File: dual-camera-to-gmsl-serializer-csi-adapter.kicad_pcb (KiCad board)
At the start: 4 copper layers, 101.2 x 43 mm, 85 parts, among them J1 Conn_FFC_WE_68715014022, J2 Conn_FFC_WE_68715014022, J3 Conn_FFC_WE_68715014022, U1 TPS2117DRLR, U2 TPS2117DRLR, U3 AP62301_TSOT

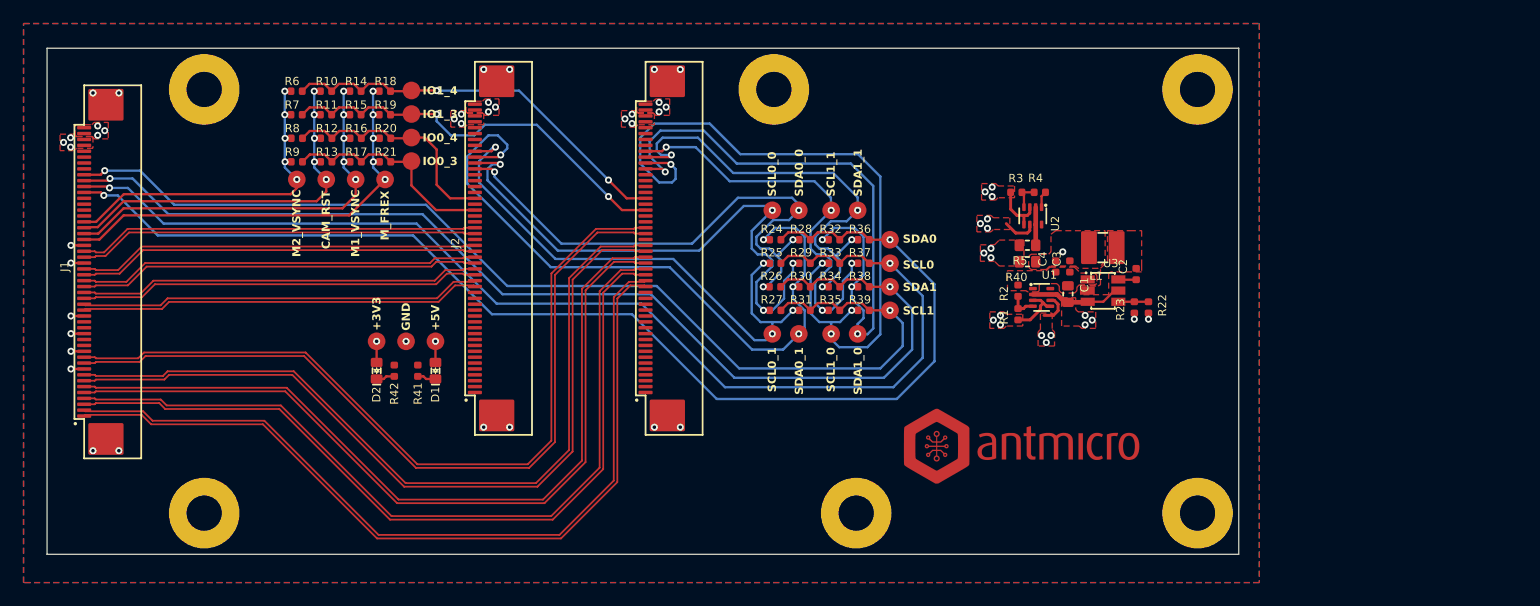
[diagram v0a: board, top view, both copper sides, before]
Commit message: [#69172] Rotate FFC connectors
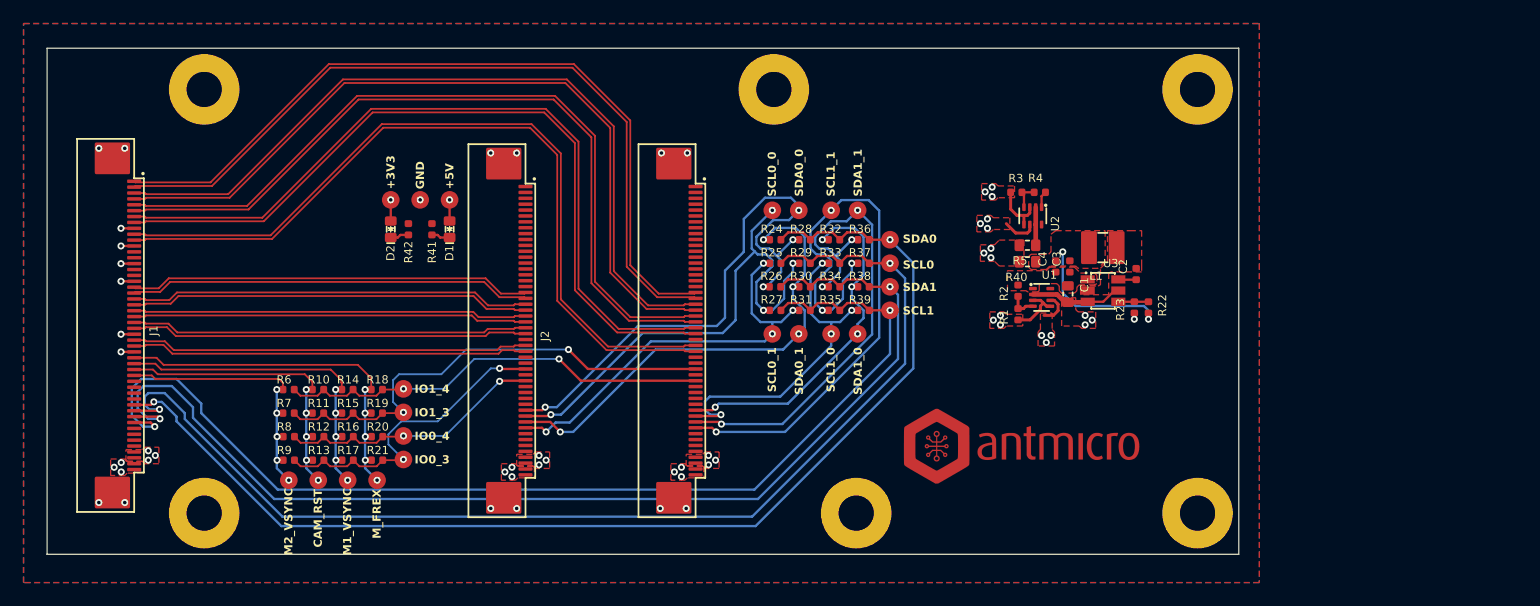
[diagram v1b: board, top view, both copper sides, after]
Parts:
- moved TP1 25.6 mm to (120.0, 116.3)
- moved TP2 25.6 mm to (122.5, 116.3)
- moved TP3 25.6 mm to (125.0, 116.3)
- moved TP4 25.6 mm to (127.5, 116.3)
- moved TP5 25.4 mm to (129.8, 108.5)
- moved TP6 25.4 mm to (129.8, 110.5)
- moved TP7 25.4 mm to (129.8, 112.5)
- moved TP8 25.4 mm to (129.8, 114.5)
- moved R10 25.4 mm to (122.5, 108.6)
- moved R11 25.4 mm to (122.5, 110.6)
- moved R12 25.4 mm to (122.5, 112.6)
- moved R13 25.4 mm to (122.5, 114.6)
- moved R14 25.4 mm to (125.0, 108.6)
- moved R15 25.4 mm to (125.0, 110.6)
- moved R16 25.4 mm to (125.0, 112.6)
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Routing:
- net /SCL_CAM1_0: track 62.0 -> 29.1 mm
- net +3V3: track 100.5 -> 128.0 mm
- net /SDA_CAM1_0: track 54.4 -> 31.0 mm
- net /5V_1: track 50.3 -> 70.9 mm
- net /SDA_CAM0_1: track 59.3 -> 41.6 mm
- net /3V3_0: track 78.2 -> 60.8 mm
- net +5V: track 137.6 -> 155.1 mm
- net /5V_0: track 80.6 -> 97.0 mm
- net /SCL_CAM1_1: track 36.5 -> 52.4 mm
- net /SCL_CAM0_1: track 47.2 -> 35.5 mm
- net /GPIO0_3: track 19.2 -> 27.2 mm, vias 0 -> 2
- net /3V3_1: track 42.6 -> 50.6 mm
- net /M1_VSYNC: track 35.8 -> 29.2 mm
- net /CAM_RST: track 32.9 -> 26.4 mm
- net /M2_VSYNC: track 30.0 -> 23.7 mm
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
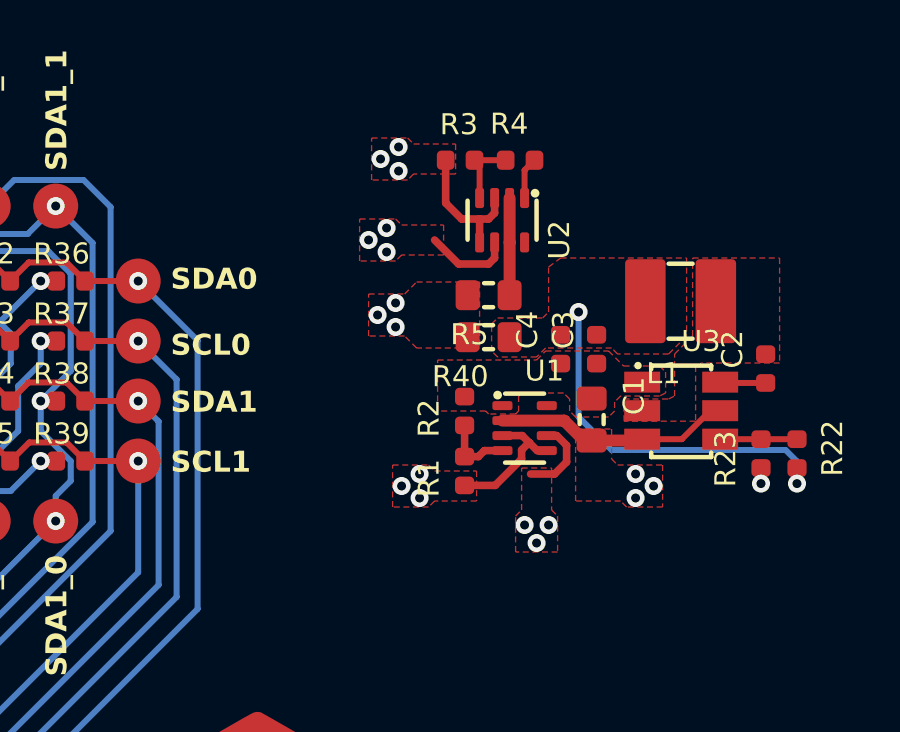
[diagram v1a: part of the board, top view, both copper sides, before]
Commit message: [#69172] Add power planes
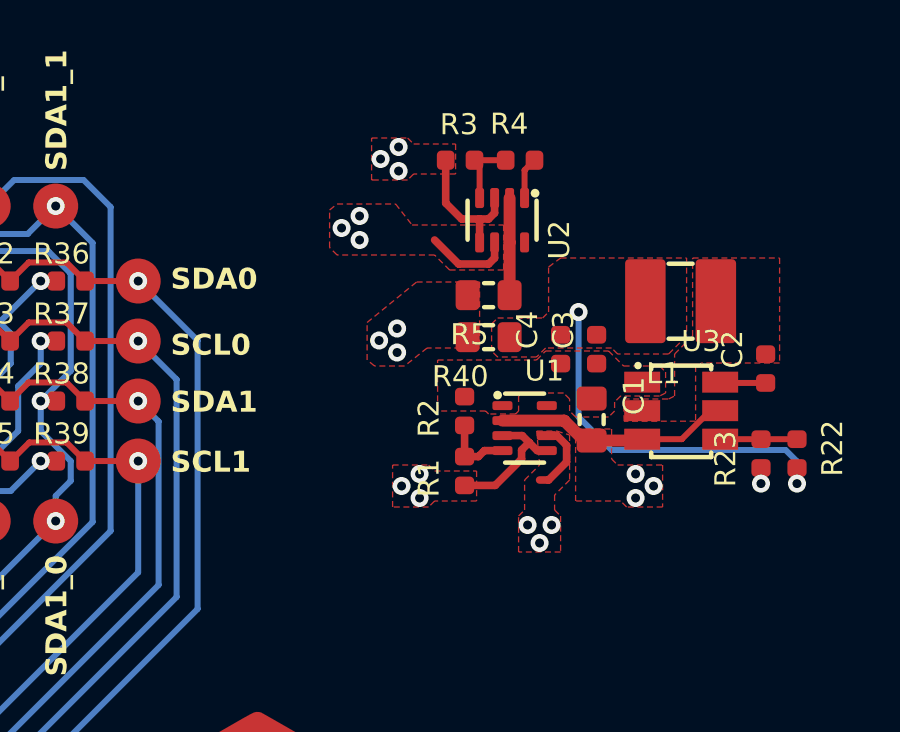
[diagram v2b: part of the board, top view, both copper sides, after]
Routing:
- net +5V: track 155.1 -> 9.75 mm
- net +3V3: track 128.0 -> 1.80 mm
- net /5V_0: track 97.0 -> 5.45 mm
- net /5V_1: track 70.9 -> 2.50 mm
- net /3V3_0: track 60.8 -> 4.64 mm
- net /3V3_1: track 50.6 -> 2.93 mm
- added copper zone on In2.Cu, net +3V3
- added copper zone on In2.Cu, net +5V
- added copper zone on In2.Cu, net /3V3_0
- added copper zone on In2.Cu, net /3V3_1
- added copper zone on In2.Cu, net /5V_0
- added copper zone on In2.Cu, net /5V_1

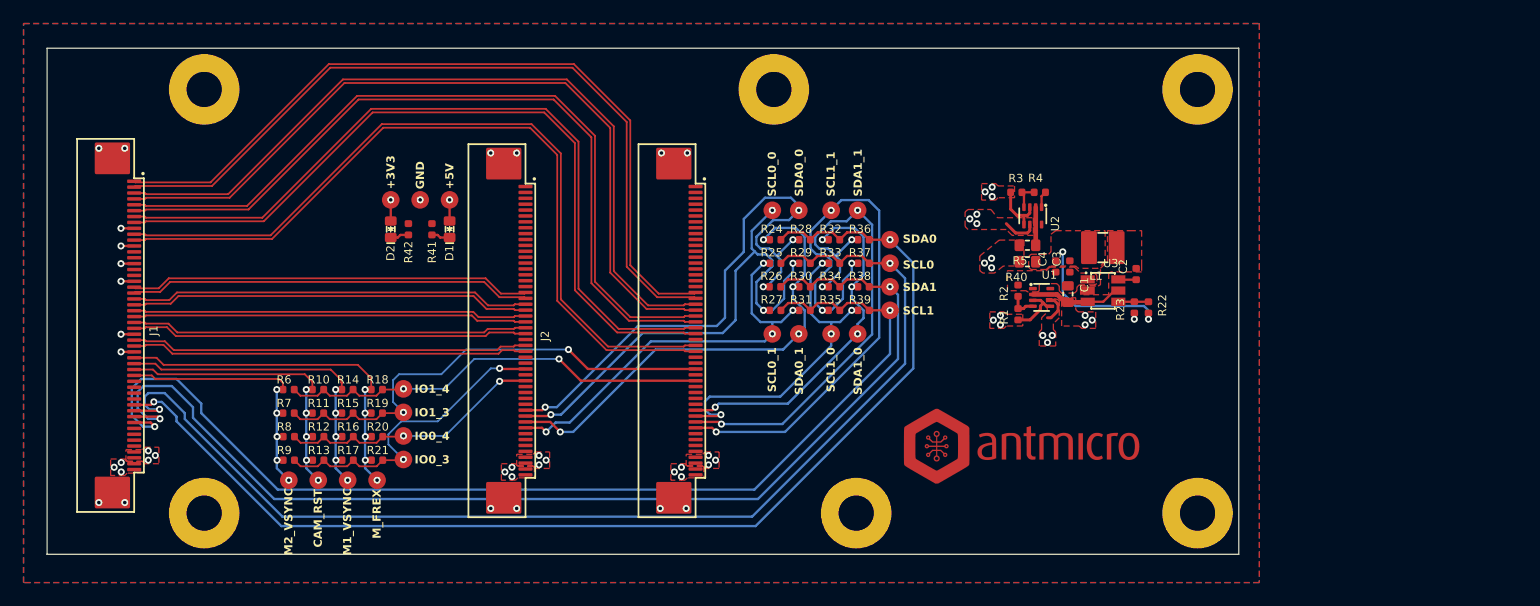
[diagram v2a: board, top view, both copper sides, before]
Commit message: [#69172] Update schematics
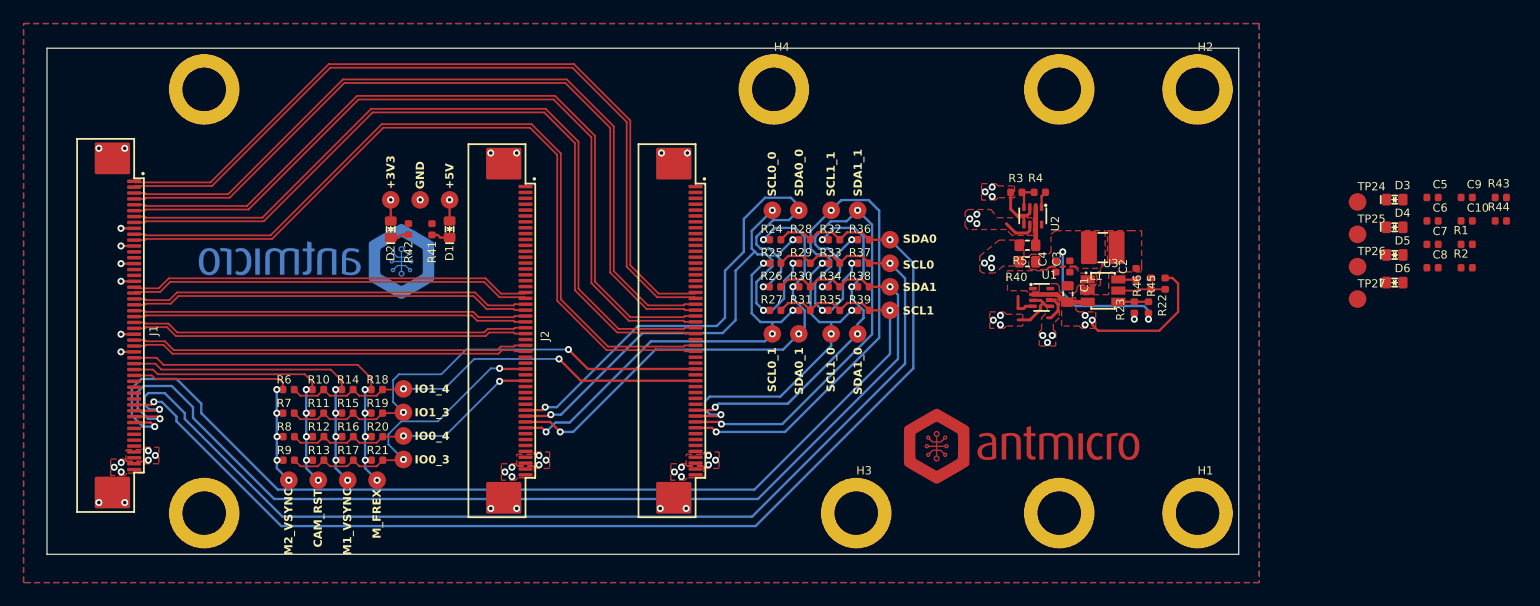
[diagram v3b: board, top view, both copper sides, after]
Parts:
- removed MP1, MP2, MP3, MP4, MP5, MP6: MP_Pad6mm_Drill3mm, antmicro-footprints:MP_Pad6mm_Drill3mm
- added C10: C_100n_0402, antmicro-footprints:C_0402_1005Metric, F.Cu at (220.1, 94.3)
- added C5: C_100n_0402, antmicro-footprints:C_0402_1005Metric, F.Cu at (217.2, 92.3)
- added C6: C_100n_0402, antmicro-footprints:C_0402_1005Metric, F.Cu at (217.2, 94.3)
- added C7: C_100n_0402, antmicro-footprints:C_0402_1005Metric, F.Cu at (217.2, 96.3)
- added C8: C_100n_0402, antmicro-footprints:C_0402_1005Metric, F.Cu at (217.2, 98.2)
- added C9: C_100n_0402, antmicro-footprints:C_0402_1005Metric, F.Cu at (220.1, 92.3)
- added D3: LED_G_0603_LTST-C190GKT, antmicro-footprints:LED_0603_1608Metric_G, F.Cu at (214.0, 92.5)
- added D4: LED_G_0603_LTST-C190GKT, antmicro-footprints:LED_0603_1608Metric_G, F.Cu at (214.0, 94.8)
- added D5: LED_G_0603_LTST-C190GKT, antmicro-footprints:LED_0603_1608Metric_G, F.Cu at (214.0, 97.2)
- added D6: LED_G_0603_LTST-C190GKT, antmicro-footprints:LED_0603_1608Metric_G, F.Cu at (214.0, 99.5)
- added H1: Spacer_Drill3.7mm_H3mm_9774030151R, antmicro-footprints:Spacer_Drill3.7mm_H3mm_9774030151R, F.Cu at (197.2, 119.1)
- added H2: Spacer_Drill3.7mm_H3mm_9774030151R, antmicro-footprints:Spacer_Drill3.7mm_H3mm_9774030151R, F.Cu at (197.2, 83.1)
- added H3: Spacer_Drill3.7mm_H3mm_9774030151R, antmicro-footprints:Spacer_Drill3.7mm_H3mm_9774030151R, F.Cu at (168.2, 119.1)
- added H4: Spacer_Drill3.7mm_H3mm_9774030151R, antmicro-footprints:Spacer_Drill3.7mm_H3mm_9774030151R, F.Cu at (161.2, 83.1)
- added H5: Spacer_Drill3.7mm_H3mm_9774030151R, antmicro-footprints:Spacer_Drill3.7mm_H3mm_9774030151R, B.Cu at (112.8, 83.1)
- added H6: Spacer_Drill3.7mm_H3mm_9774030151R, antmicro-footprints:Spacer_Drill3.7mm_H3mm_9774030151R, B.Cu at (112.8, 119.1)
- added H7: Spacer_Drill3.7mm_H3mm_9774030151R, antmicro-footprints:Spacer_Drill3.7mm_H3mm_9774030151R, B.Cu at (185.5, 83.1)
- added H8: Spacer_Drill3.7mm_H3mm_9774030151R, antmicro-footprints:Spacer_Drill3.7mm_H3mm_9774030151R, B.Cu at (185.5, 119.1)
- added R43: R_12k_0402, antmicro-footprints:R_0402_1005Metric, F.Cu at (223.0, 92.3)
- added R44: R_12k_0402, antmicro-footprints:R_0402_1005Metric, F.Cu at (223.0, 94.3)
- added R45: R_0R_0402, antmicro-footprints:R_0402_1005Metric, F.Cu at (194.5, 99.6)
- added R46: R_0R_0402, antmicro-footprints:R_0402_1005Metric, F.Cu at (193.3, 99.6)
- added REF**: antmicro-logo_scaled_20mm, antmicro-footprints:antmicro-logo_scaled_20mm, B.Cu at (122.4, 97.9)
- added TP24: TP_1.5mm_SMD, antmicro-footprints:TP_SMD_1.5mm, F.Cu at (210.8, 92.7)
- added TP25: TP_1.5mm_SMD, antmicro-footprints:TP_SMD_1.5mm, F.Cu at (210.8, 95.4)
- added TP26: TP_1.5mm_SMD, antmicro-footprints:TP_SMD_1.5mm, F.Cu at (210.8, 98.2)
- added TP27: TP_1.5mm_SMD, antmicro-footprints:TP_SMD_1.5mm, F.Cu at (210.8, 100.9)
- R1: value R_34k_0402 -> R_470R_0402
- R11, R13, R15, R17, R19, R21, R7, R9: value R_0R_0402 -> R_10k_0402
- R2, R4: value R_10k_0402 -> R_200R_0402
- R3: value R_18k_0402 -> R_470R_0402
- R42: value R_470R_0402 -> R_200R_0402
- moved R1 38.6 mm to (220.1, 96.3), turned to 0 degrees
- moved R2 38.2 mm to (220.1, 98.2), turned to 0 degrees
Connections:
- R1 pad 1: Net-(U1-PR1) -> GND
- R1 pad 2: /5V_0 -> Net-(D3-C)
- R11 pad 1: /GPIO1_3 -> /CAM_RST
- R11 pad 2: /CAM_RST -> /GPIO1_3
- R13 pad 1: /GPIO0_3 -> /CAM_RST
- R13 pad 2: /CAM_RST -> /GPIO0_3
- R15 pad 1: /GPIO1_3 -> /M1_VSYNC
- R15 pad 2: /M1_VSYNC -> /GPIO1_3
- R17 pad 1: /GPIO0_3 -> /M1_VSYNC
- R17 pad 2: /M1_VSYNC -> /GPIO0_3
- R19 pad 1: /GPIO1_3 -> /M_FREX
- R19 pad 2: /M_FREX -> /GPIO1_3
- R2 pad 2: Net-(U1-PR1) -> Net-(D2-C)
- R21 pad 1: /GPIO0_3 -> /M_FREX
- R21 pad 2: /M_FREX -> /GPIO0_3
- R3 pad 1: Net-(U2-PR1) -> GND
- R3 pad 2: /3V3_0 -> Net-(D5-C)
- R4 pad 2: Net-(U2-PR1) -> Net-(D4-C)
- R42 pad 2: Net-(D2-C) -> Net-(D6-C)
- R7 pad 1: /GPIO1_3 -> /M2_VSYNC
- R7 pad 2: /M2_VSYNC -> /GPIO1_3
- R9 pad 1: /GPIO0_3 -> /M2_VSYNC
- R9 pad 2: /M2_VSYNC -> /GPIO0_3
- U1 pad 4: Net-(U1-PR1) -> GND
- U1 pad 5: /5V_0 -> GND
- U2 pad 4: Net-(U2-PR1) -> GND
- U2 pad 5: /3V3_0 -> GND
- U3 pad 5: +5V -> /EN_3V3
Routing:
- net +5V: track 9.75 -> 19.0 mm
- net GND: track 8.64 -> 13.4 mm
- net /EN_3V3: track 0.00 -> 4.03 mm
- net Net-(U1-PR1): track 2.38 -> 0.00 mm
- net Net-(U2-PR1): track 2.37 -> 0.00 mm

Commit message: [#69172] Update PCB
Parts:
- removed the REF** at (182.3, 113.6)
- added G***: LOGO, antmicro-footprints:antmicro-logo_scaled_12mm_silk, F.Cu at (124.4, 84.4)
- added REF**: OSHW-Logo_5.7x6mm_SilkScreen, antmicro-footprints:OSHW-Logo_5.7x6mm_SilkScreen, F.Cu at (114.4, 103.8)
- moved C6 110.8 mm to (108.7, 116.2), turned to 90 degrees
- moved C5 109.9 mm to (109.8, 115.2), turned to 90 degrees
- moved R44 107.4 mm to (117.6, 114.6)
- moved R43 107.1 mm to (117.5, 110.6)
- moved R1 98.7 mm to (121.5, 92.8), turned to -90 degrees
- moved D3 92.5 mm to (121.5, 95.0), turned to -90 degrees
- moved D5 90.5 mm to (123.5, 95.0), turned to -90 degrees
- moved TP24 89.5 mm to (121.5, 97.2), turned to 90 degrees
- moved R2 88.8 mm to (131.5, 92.8), turned to -90 degrees
- moved TP26 87.3 mm to (123.5, 97.2), turned to 90 degrees
- moved D4 86.5 mm to (127.5, 95.0), turned to -90 degrees
- moved D6 84.6 mm to (129.5, 95.0), turned to -90 degrees
- moved TP25 83.4 mm to (127.5, 97.2), turned to 90 degrees
- moved TP27 81.4 mm to (129.5, 97.2), turned to 90 degrees
- moved C8 77.5 mm to (141.9, 116.6), turned to 90 degrees
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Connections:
- net /CAM_RST renamed /CAM_FFC_PIN33
- net /M1_VSYNC renamed /CAM_FFC_PIN32
- net /M2_VSYNC renamed /CAM_FFC_PIN34
- net /M_FREX renamed /CAM_FFC_PIN31
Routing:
- net /3V3_1: track 2.93 -> 65.9 mm, vias 6 -> 7
- net /5V_1: track 2.50 -> 64.0 mm, vias 6 -> 7
- net +3V3: track 1.80 -> 48.4 mm
- net +5V: track 19.0 -> 62.1 mm
- net /3V3_0: track 4.64 -> 44.9 mm, vias 6 -> 7
- net /5V_0: track 5.45 -> 42.0 mm, vias 6 -> 7
- net GND: track 13.4 -> 18.9 mm, vias 20 -> 86
- net /CSI1.D0_N: track 66.7 -> 69.8 mm
- net /CSI1.D0_P: track 66.7 -> 69.8 mm
- net /CSI1.D1_N: track 66.7 -> 69.8 mm
- net /CSI1.D1_P: track 66.7 -> 69.8 mm
- net /CSI1.CLK_P: track 66.8 -> 69.8 mm
- net /CSI1.CLK_N: track 66.8 -> 69.8 mm
- net /GPIO1_3: track 41.2 -> 44.1 mm
- net /GPIO0_3: track 27.2 -> 30.1 mm
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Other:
- board text added: "+3V3_0"
- board text added: "+3V3_1"
- board text added: "+5V_0"
- board text added: "+5V_1"
- board text added: "1"
- board text added: "CAMERA"
- board text added: "Dual Camera to GMSL Serializer CSI adapter Rev. ${REVISION} 11/2024"
- board text added: "FFC_31"
- board text added: "FFC_32"
- board text added: "FFC_33"
- board text added: "FFC_34"
- board text added: "GMSL SERIALIZER 1"
- board text added: "GMSL SERIALIZER 2"
- board text added: "PCB SHA: ########"
- board text removed: "CAM_RST"
- board text removed: "M1_VSYNC"
- board text removed: "M2_VSYNC"
- board text removed: "M_FREX"
